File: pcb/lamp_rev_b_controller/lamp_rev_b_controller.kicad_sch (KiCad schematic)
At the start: 0 parts

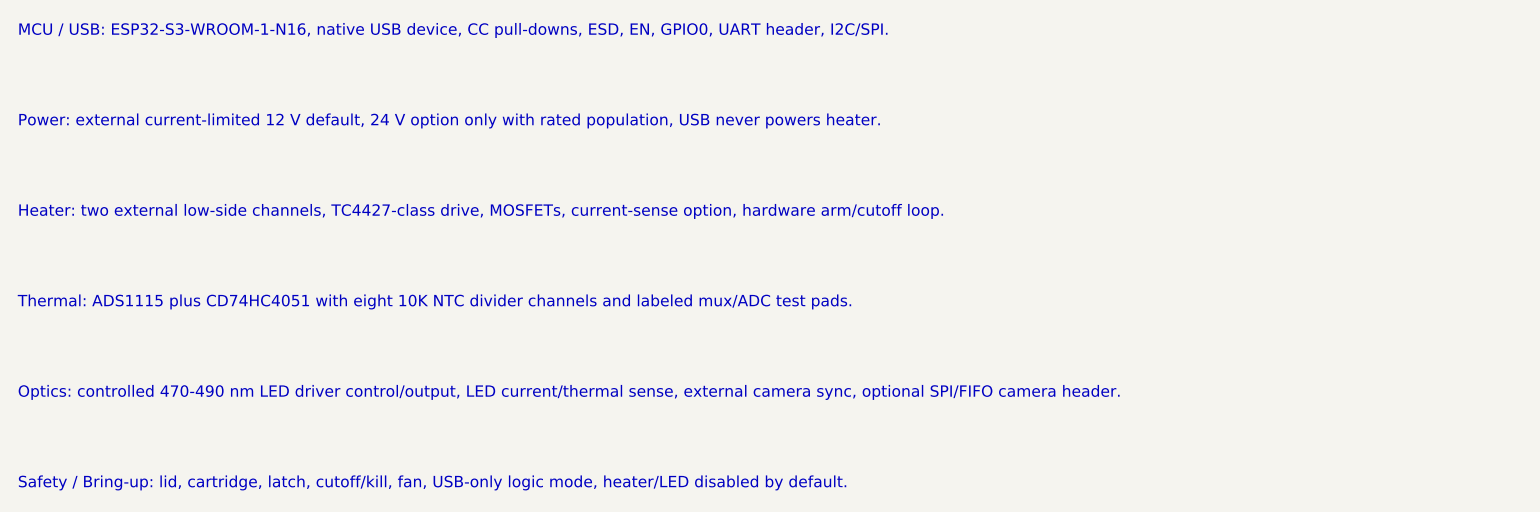
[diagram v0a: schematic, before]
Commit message: Resolve Rev B controller PCBA selection blockers
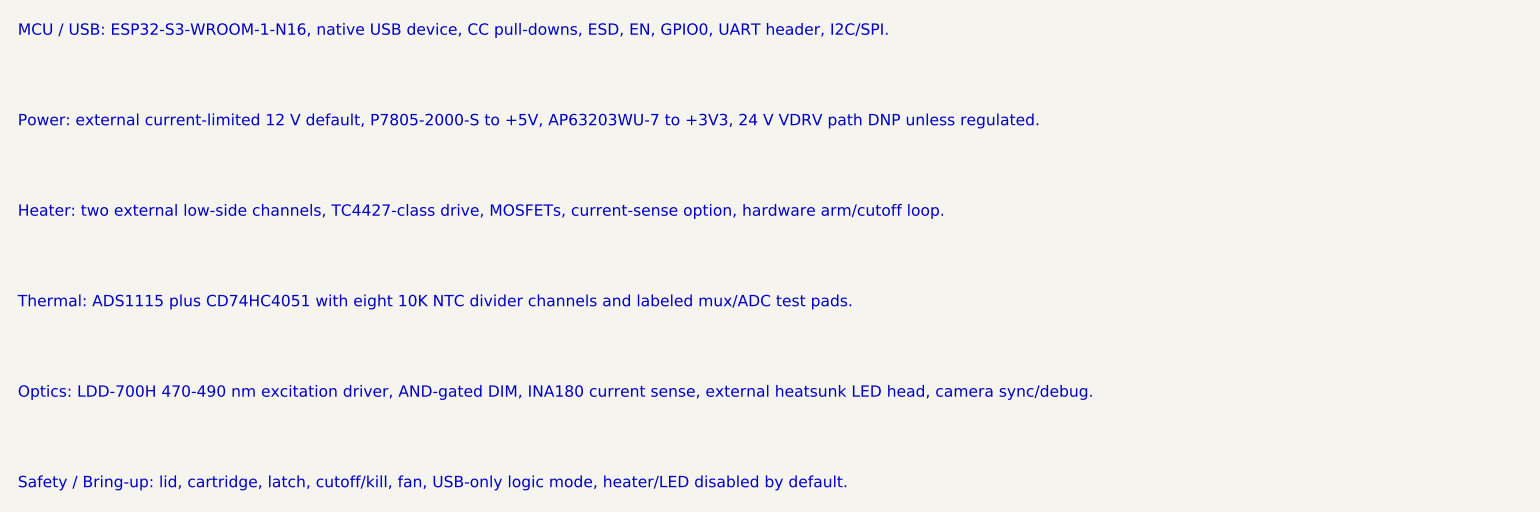
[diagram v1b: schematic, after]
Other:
- note added: "Optics: LDD-700H 470-490 nm excitation driver, AND-gated DIM, INA180 current sense, external heatsunk LED head, camera sync/debug."
- note added: "Power: external current-limited 12 V default, P7805-2000-S to +5V, AP63203WU-7 to +3V3, 24 V VDRV path DNP unless regulated."
- note removed: "Optics: controlled 470-490 nm LED driver control/output, LED current/thermal sense, external camera sync, optional SPI/FIFO camera header."
- note removed: "Power: external current-limited 12 V default, 24 V option only with rated population, USB never powers heater."
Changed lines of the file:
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@@
     (effects (font (size 1.27 1.27)) (justify left))
   )
-  (text "Power: external current-limited 12 V default, 24 V option only with rated population, USB never powers heater."
+  (text "Power: external current-limited 12 V default, P7805-2000-S to +5V, AP63203WU-7 to +3V3, 24 V VDRV path DNP unless regulated."
     (at 20.32 35.56 0)
     (effects (font (size 1.27 1.27)) (justify left))
@@
     (effects (font (size 1.27 1.27)) (justify left))
   )
-  (text "Optics: controlled 470-490 nm LED driver control/output, LED current/thermal sense, external camera sync, optional SPI/FIFO camera header."
+  (text "Optics: LDD-700H 470-490 nm excitation driver, AND-gated DIM, INA180 current sense, external heatsunk LED head, camera sync/debug."
     (at 20.32 66.04 0)
     (effects (font (size 1.27 1.27)) (justify left))

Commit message: Implement Rev B controller schematic capture gate
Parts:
- added C1: 22uF rail bulk, lcsc:C1206, symbol LF_CAPTURE_C1
- added C10: 100nF, lcsc:C0603, symbol LF_CAPTURE_C10
- added C11: 100nF, lcsc:C0603, symbol LF_CAPTURE_C11
- added C12: 100nF, lcsc:C0603, symbol LF_CAPTURE_C12
- added C13: 100nF, lcsc:C0603, symbol LF_CAPTURE_C13
- added C14: 100nF, lcsc:C0603, symbol LF_CAPTURE_C14
- added C15: 100nF, lcsc:C0603, symbol LF_CAPTURE_C15
- added C16: 100nF, lcsc:C0603, symbol LF_CAPTURE_C16
- added C17: 100nF, lcsc:C0603, symbol LF_CAPTURE_C17
- added C2: 22uF >=10V +5V buck output, lcsc:C1206, symbol LF_CAPTURE_C2
- added C3: 22uF AP63203 input, lcsc:C1206, symbol LF_CAPTURE_C3
- added C4: 22uF 50V VIN buck input, lcsc:C1206, symbol LF_CAPTURE_C4
- added C5: 22uF rail bulk, lcsc:C1206, symbol LF_CAPTURE_C5
- added C6: 22uF rail bulk, lcsc:C1206, symbol LF_CAPTURE_C6
- added C7: 22uF AP63203 output, lcsc:C1206, symbol LF_CAPTURE_C7
- added C8: 22uF AP63203 output, lcsc:C1206, symbol LF_CAPTURE_C8
- added C9: 100nF bootstrap, lcsc:C0603, symbol LF_CAPTURE_C9
- added D1: SMBJ18A footprint option, lcsc:SMB_L4.6-W3.6-LS5.3-RD, symbol LF_CAPTURE_D1
- added D2: LED0603 status, lcsc:LED0603-RD, symbol LF_CAPTURE_D2
- added D3: LED0603 status, lcsc:LED0603-RD, symbol LF_CAPTURE_D3
- added F1: RUEF500K/PTC, lcsc:FUSE2920, symbol LF_CAPTURE_F1
- added J1: TYPE-C 3.1 MT 16P, lcsc:USB-C-SMD_TYPE-C-USB-4, symbol LF_CAPTURE_J1
- added J10: 2-pin NTC header, lcsc:PINHEADER_1X02_2.54MM, symbol LF_CAPTURE_J10
- added J11: 2-pin NTC header, lcsc:PINHEADER_1X02_2.54MM, symbol LF_CAPTURE_J11
- added J12: DB128H-5.08-2P-BK-S, lcsc:TERM-BLOCK-5.08-2P, symbol LF_CAPTURE_J12
- added J13: DB128H-5.08-2P-BK-S, lcsc:TERM-BLOCK-5.08-2P, symbol LF_CAPTURE_J13
- added J15: DB128H-5.08-2P-BK-S, lcsc:TERM-BLOCK-5.08-2P, symbol LF_CAPTURE_J15
- added J16: LED NTC/ID header, lcsc:PINHEADER_1X04_2.54MM, symbol LF_CAPTURE_J16
- added J17: External camera sync header, lcsc:PINHEADER_1X06_2.54MM, symbol LF_CAPTURE_J17
- added J18: SPI/FIFO camera module header, lcsc:PINHEADER_2X06_2.54MM, symbol LF_CAPTURE_J18
- added J19: Lid/cartridge/cutoff interlock header, lcsc:PINHEADER_1X06_2.54MM, symbol LF_CAPTURE_J19
- added J2: DB128H-5.08-2P-BK-S, lcsc:TERM-BLOCK-5.08-2P, symbol LF_CAPTURE_J2
- added J20: Fan PWM/tach header, lcsc:PINHEADER_1X04_2.54MM, symbol LF_CAPTURE_J20
- added J21: 2x3 UART/programming header, lcsc:PINHEADER_2X03_2.54MM, symbol LF_CAPTURE_J21
- added J22: I2C expansion header, lcsc:PINHEADER_1X04_2.54MM, symbol LF_CAPTURE_J22
- added J23: Analog optical diagnostic header, lcsc:PINHEADER_1X06_2.54MM, symbol LF_CAPTURE_J23
- added J4: 2-pin NTC header, lcsc:PINHEADER_1X02_2.54MM, symbol LF_CAPTURE_J4
- added J5: 2-pin NTC header, lcsc:PINHEADER_1X02_2.54MM, symbol LF_CAPTURE_J5
- added J6: 2-pin NTC header, lcsc:PINHEADER_1X02_2.54MM, symbol LF_CAPTURE_J6
- added J7: 2-pin NTC header, lcsc:PINHEADER_1X02_2.54MM, symbol LF_CAPTURE_J7
- added J8: 2-pin NTC header, lcsc:PINHEADER_1X02_2.54MM, symbol LF_CAPTURE_J8
- added J9: 2-pin NTC header, lcsc:PINHEADER_1X02_2.54MM, symbol LF_CAPTURE_J9
- added L1: Wurth 74439346068 6.8uH shielded inductor, lcsc:IND_74439346068, symbol LF_CAPTURE_L1
- added Q1: IRLB3813PBF TO-220 12V prototype, lcsc:TO-220-3_VERTICAL, symbol LF_CAPTURE_Q1
- added Q2: IRLB3813PBF TO-220 12V prototype, lcsc:TO-220-3_VERTICAL, symbol LF_CAPTURE_Q2
- added R1: 5.1k, lcsc:R0805, symbol LF_CAPTURE_R1
- added R10: 10k 0.1%, lcsc:R0805, symbol LF_CAPTURE_R10
- added R11: 10k 0.1%, lcsc:R0805, symbol LF_CAPTURE_R11
- added R12: 10k 0.1%, lcsc:R0805, symbol LF_CAPTURE_R12
- added R13: 10k 0.1%, lcsc:R0805, symbol LF_CAPTURE_R13
- added R14: 10k 0.1%, lcsc:R0805, symbol LF_CAPTURE_R14
- added R15: 10k 0.1%, lcsc:R0805, symbol LF_CAPTURE_R15
- added R16: 10k 0.1%, lcsc:R0805, symbol LF_CAPTURE_R16
- added R17: 10k 0.1%, lcsc:R0805, symbol LF_CAPTURE_R17
- added R2: 5.1k, lcsc:R0805, symbol LF_CAPTURE_R2
- added R20: 33R, lcsc:R0805, symbol LF_CAPTURE_R20
- added R21: 33R, lcsc:R0805, symbol LF_CAPTURE_R21
- added R22: 10k, lcsc:R0805, symbol LF_CAPTURE_R22
- added R23: 10k, lcsc:R0805, symbol LF_CAPTURE_R23
- added R24: 10k, lcsc:R0805, symbol LF_CAPTURE_R24
- added R25: 50mR DNP option, lcsc:R0805, symbol LF_CAPTURE_R25
- added R26: 50mR DNP option, lcsc:R0805, symbol LF_CAPTURE_R26
- added R3: 100k/100k VBUS sense, lcsc:R0805, symbol LF_CAPTURE_R3
- added R30: 1k, lcsc:R0805, symbol LF_CAPTURE_R30
- added R31: 1k, lcsc:R0805, symbol LF_CAPTURE_R31
- added R4: 100k/100k VBUS sense, lcsc:R0805, symbol LF_CAPTURE_R4
- added R40: 4.7k, lcsc:R0805, symbol LF_CAPTURE_R40
- added R41: 4.7k, lcsc:R0805, symbol LF_CAPTURE_R41
- added R42: 4.7k, lcsc:R0805, symbol LF_CAPTURE_R42
- added R43: 4.7k, lcsc:R0805, symbol LF_CAPTURE_R43
- added R44: 4.7k, lcsc:R0805, symbol LF_CAPTURE_R44
- added R45: 4.7k, lcsc:R0805, symbol LF_CAPTURE_R45
- added R46: 4.7k, lcsc:R0805, symbol LF_CAPTURE_R46
- added R47: 4.7k, lcsc:R0805, symbol LF_CAPTURE_R47
- added R48: 10k, lcsc:R0805, symbol LF_CAPTURE_R48
- added R49: 10k, lcsc:R0805, symbol LF_CAPTURE_R49
- added R50: 100R LED DIM series, lcsc:R0805, symbol LF_CAPTURE_R50
- added R51: 100k LED DIM pulldown, lcsc:R0805, symbol LF_CAPTURE_R51
- added R52: 0R LED_SUPPLY feed link from VIN_PROTECTED, lcsc:R0805, symbol LF_CAPTURE_R52
- added R53: 0.1R 1% >=1W LED current shunt, lcsc:R2512, symbol LF_CAPTURE_R53
- added R54: 10k LED_FAULT_N pull-up, lcsc:R0805, symbol LF_CAPTURE_R54
- added TP_3V3: test point +3V3, lcsc:TESTPOINT_SMD_1.5MM, symbol LF_CAPTURE_TP_3V3
- added TP_3V3A: test point +3V3_ANA, lcsc:TESTPOINT_SMD_1.5MM, symbol LF_CAPTURE_TP_3V3A
- added TP_5V: test point +5V, lcsc:TESTPOINT_SMD_1.5MM, symbol LF_CAPTURE_TP_5V
- added TP_ADS_AIN0: test point ADS_AIN0, lcsc:TESTPOINT_SMD_1.5MM, symbol LF_CAPTURE_TP_ADS_AIN0
- added TP_ADS_AIN1: test point ADS_AIN1, lcsc:TESTPOINT_SMD_1.5MM, symbol LF_CAPTURE_TP_ADS_AIN1
- added TP_ADS_AIN2: test point ADS_AIN2, lcsc:TESTPOINT_SMD_1.5MM, symbol LF_CAPTURE_TP_ADS_AIN2
- added TP_ADS_AIN3: test point ADS_AIN3, lcsc:TESTPOINT_SMD_1.5MM, symbol LF_CAPTURE_TP_ADS_AIN3
- added TP_AUX_ANALOG: test point AUX_ANALOG_IN, lcsc:TESTPOINT_SMD_1.5MM, symbol LF_CAPTURE_TP_AUX_ANALOG
- added TP_BOOT: test point ESP_GPIO0_BOOT, lcsc:TESTPOINT_SMD_1.5MM, symbol LF_CAPTURE_TP_BOOT
- added TP_CAM_CS: test point CAM_CS_N, lcsc:TESTPOINT_SMD_1.5MM, symbol LF_CAPTURE_TP_CAM_CS
- added TP_CAM_FRAME: test point CAM_FRAME_INT, lcsc:TESTPOINT_SMD_1.5MM, symbol LF_CAPTURE_TP_CAM_FRAME
- added TP_CAM_PWDN: test point CAM_PWDN_N, lcsc:TESTPOINT_SMD_1.5MM, symbol LF_CAPTURE_TP_CAM_PWDN
- added TP_CAM_RESET: test point CAM_RESET_N, lcsc:TESTPOINT_SMD_1.5MM, symbol LF_CAPTURE_TP_CAM_RESET
- added TP_CART: test point CART_PRESENT_N, lcsc:TESTPOINT_SMD_1.5MM, symbol LF_CAPTURE_TP_CART
- added TP_CUTOFF: test point AUX_IO0_THERMAL_CUTOFF_OK, lcsc:TESTPOINT_SMD_1.5MM, symbol LF_CAPTURE_TP_CUTOFF
- added TP_EN: test point ESP_EN, lcsc:TESTPOINT_SMD_1.5MM, symbol LF_CAPTURE_TP_EN
- added TP_EXPOSURE: test point EXPOSURE_ACTIVE_IN, lcsc:TESTPOINT_SMD_1.5MM, symbol LF_CAPTURE_TP_EXPOSURE
- added TP_FAN_PWM: test point FAN_PWM, lcsc:TESTPOINT_SMD_1.5MM, symbol LF_CAPTURE_TP_FAN_PWM
- added TP_FAN_TACH: test point FAN_TACH, lcsc:TESTPOINT_SMD_1.5MM, symbol LF_CAPTURE_TP_FAN_TACH
- added TP_FAULT: test point STATUS_FAULT_LED, lcsc:TESTPOINT_SMD_1.5MM, symbol LF_CAPTURE_TP_FAULT
- added TP_FRAME_TRIG: test point FRAME_TRIG_OUT, lcsc:TESTPOINT_SMD_1.5MM, symbol LF_CAPTURE_TP_FRAME_TRIG
- added TP_GND: test point GND, lcsc:TESTPOINT_SMD_1.5MM, symbol LF_CAPTURE_TP_GND
- added TP_HEATER0_GATE: test point HEATER0_GATE, lcsc:TESTPOINT_SMD_1.5MM, symbol LF_CAPTURE_TP_HEATER0_GATE
- added TP_HEATER0_LOW: test point HEATER0_LOW, lcsc:TESTPOINT_SMD_1.5MM, symbol LF_CAPTURE_TP_HEATER0_LOW
- added TP_HEATER0_PWM: test point HEATER0_PWM, lcsc:TESTPOINT_SMD_1.5MM, symbol LF_CAPTURE_TP_HEATER0_PWM
- added TP_HEATER1_GATE: test point HEATER1_GATE, lcsc:TESTPOINT_SMD_1.5MM, symbol LF_CAPTURE_TP_HEATER1_GATE
- added TP_HEATER1_LOW: test point HEATER1_LOW, lcsc:TESTPOINT_SMD_1.5MM, symbol LF_CAPTURE_TP_HEATER1_LOW
- added TP_HEATER1_PWM: test point HEATER1_PWM, lcsc:TESTPOINT_SMD_1.5MM, symbol LF_CAPTURE_TP_HEATER1_PWM
- added TP_HEATER_ARM: test point HEATER_ARM, lcsc:TESTPOINT_SMD_1.5MM, symbol LF_CAPTURE_TP_HEATER_ARM
- added TP_HEATER_SENSE: test point HEATER_SUPPLY_SENSE, lcsc:TESTPOINT_SMD_1.5MM, symbol LF_CAPTURE_TP_HEATER_SENSE
- added TP_I2C_SCL: test point I2C_SCL, lcsc:TESTPOINT_SMD_1.5MM, symbol LF_CAPTURE_TP_I2C_SCL
- added TP_I2C_SDA: test point I2C_SDA, lcsc:TESTPOINT_SMD_1.5MM, symbol LF_CAPTURE_TP_I2C_SDA
- added TP_LATCH: test point LATCH_LOCKED_N, lcsc:TESTPOINT_SMD_1.5MM, symbol LF_CAPTURE_TP_LATCH
- added TP_LED_EN: test point LED_EXC_EN, lcsc:TESTPOINT_SMD_1.5MM, symbol LF_CAPTURE_TP_LED_EN
- added TP_LED_PWM: test point LED_EXC_PWM, lcsc:TESTPOINT_SMD_1.5MM, symbol LF_CAPTURE_TP_LED_PWM
- added TP_LED_SENSE: test point LED_CURRENT_SENSE, lcsc:TESTPOINT_SMD_1.5MM, symbol LF_CAPTURE_TP_LED_SENSE
- added TP_LED_SUPPLY: test point LED_SUPPLY, lcsc:TESTPOINT_SMD_1.5MM, symbol LF_CAPTURE_TP_LED_SUPPLY
- added TP_LED_SYNC: test point LED_SYNC_OUT, lcsc:TESTPOINT_SMD_1.5MM, symbol LF_CAPTURE_TP_LED_SYNC
- added TP_LID: test point LID_CLOSED_N, lcsc:TESTPOINT_SMD_1.5MM, symbol LF_CAPTURE_TP_LID
- added TP_RUN: test point STATUS_RUN_LED, lcsc:TESTPOINT_SMD_1.5MM, symbol LF_CAPTURE_TP_RUN
- added TP_SD_CS: test point SD_CS_N, lcsc:TESTPOINT_SMD_1.5MM, symbol LF_CAPTURE_TP_SD_CS
- added TP_SPARE42: test point SPARE_GPIO42, lcsc:TESTPOINT_SMD_1.5MM, symbol LF_CAPTURE_TP_SPARE42
- added TP_SPI_MISO: test point SPI_MISO, lcsc:TESTPOINT_SMD_1.5MM, symbol LF_CAPTURE_TP_SPI_MISO
- added TP_SPI_MOSI: test point SPI_MOSI, lcsc:TESTPOINT_SMD_1.5MM, symbol LF_CAPTURE_TP_SPI_MOSI
- added TP_SPI_SCLK: test point SPI_SCLK, lcsc:TESTPOINT_SMD_1.5MM, symbol LF_CAPTURE_TP_SPI_SCLK
- added TP_THERM_EN: test point THERM_MUX_EN_N, lcsc:TESTPOINT_SMD_1.5MM, symbol LF_CAPTURE_TP_THERM_EN
- added TP_THERM_OUT: test point THERM_MUX_OUT, lcsc:TESTPOINT_SMD_1.5MM, symbol LF_CAPTURE_TP_THERM_OUT
- added TP_THERM_S0: test point THERM_MUX_S0, lcsc:TESTPOINT_SMD_1.5MM, symbol LF_CAPTURE_TP_THERM_S0
- added TP_THERM_S1: test point THERM_MUX_S1, lcsc:TESTPOINT_SMD_1.5MM, symbol LF_CAPTURE_TP_THERM_S1
- added TP_THERM_S2: test point THERM_MUX_S2, lcsc:TESTPOINT_SMD_1.5MM, symbol LF_CAPTURE_TP_THERM_S2
- added TP_UART_RX: test point UART0_RXD, lcsc:TESTPOINT_SMD_1.5MM, symbol LF_CAPTURE_TP_UART_RX
- added TP_UART_TX: test point UART0_TXD, lcsc:TESTPOINT_SMD_1.5MM, symbol LF_CAPTURE_TP_UART_TX
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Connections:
- new net +3V3: C7.1 (+3V3), C8.1 (+3V3), D2.2 (+3V3), D3.2 (+3V3), J17.2 (+3V3), J18.3 (SPI_SCLK), J19.5 (+3V3), J21.2 (+3V3), J22.4 (GND), L1.2 (+3V3), R40.2 (+3V3), R41.2 (+3V3)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
- new net +3V3_ANA: C5.1 (+3V3_ANA), J16.4 (GND), J23.3 (ADS_AIN3), TP_3V3A.1 (+3V3_ANA), U5.1 (THERM_CH_4)
- new net +5V: C2.1 (+5V), C3.1 (+5V), J20.4 (GND), TP_5V.1 (+5V), U3.2 (+5V), U3.6 (3V3_BST)
- new net 3V3_BST: C9.1 (3V3_BST), U3.4 (+5V)
- new net 3V3_SW: C9.2 (3V3_SW), L1.1 (3V3_SW), U3.5 (3V3_SW)
- new net ADS_AIN0: TP_ADS_AIN0.1 (ADS_AIN0), U4.1 (GND)
- new net ADS_AIN1: TP_ADS_AIN1.1 (ADS_AIN1), U4.9 (I2C_SDA)
- new net ADS_AIN2: TP_ADS_AIN2.1 (ADS_AIN2), U4.8 (+3V3)
- new net ADS_AIN3: J23.1 (+3V3_ANA), TP_ADS_AIN3.1 (ADS_AIN3), U4.7 (ADS_AIN3)
- new net AUX_ANALOG_IN: J16.1 (THERM_CH_5), J23.6 (I2C_SCL), TP_AUX_ANALOG.1 (AUX_ANALOG_IN)
- new net AUX_IO0_THERMAL_CUTOFF_OK: J19.6 (GND), R47.1 (AUX_IO0_THERMAL_CUTOFF_OK), TP_CUTOFF.1 (AUX_IO0_THERMAL_CUTOFF_OK), U1.6 (THERM_MUX_S2)
- new net CAM_CS_N: J18.7 (CAM_FRAME_INT), R42.1 (CAM_CS_N), TP_CAM_CS.1 (CAM_CS_N), U1.17 (SPI_SCLK)
- new net CAM_FRAME_INT: J18.6 (CAM_CS_N), TP_CAM_FRAME.1 (CAM_FRAME_INT), U1.16 (NC_16)
- new net CAM_PWDN_N: J18.4 (SPI_MOSI), TP_CAM_PWDN.1 (CAM_PWDN_N), U1.15 (NC_15)
- new net CAM_RESET_N: J18.5 (SPI_MISO), TP_CAM_RESET.1 (CAM_RESET_N), U1.30 (LID_CLOSED_N)
- new net CART_PRESENT_N: J19.2 (CART_PRESENT_N), R45.1 (CART_PRESENT_N), TP_CART.1 (CART_PRESENT_N), U1.7 (LED_EXC_PWM)
- new net ESP_EN: J21.5 (ESP_EN), R48.1 (ESP_EN), TP_EN.1 (ESP_EN), U1.9 (HEATER_ARM)
- new net ESP_GPIO0_BOOT: J21.4 (UART0_RXD), R49.1 (ESP_GPIO0_BOOT), TP_BOOT.1 (ESP_GPIO0_BOOT), U1.10 (HEATER0_PWM)
- new net EXPOSURE_ACTIVE_IN: J17.6 (SPARE_GPIO42), TP_EXPOSURE.1 (EXPOSURE_ACTIVE_IN)
- new net FAN_PWM: J20.2 (FAN_TACH), TP_FAN_PWM.1 (FAN_PWM)
- new net FAN_TACH: J20.1 (FAN_PWM), TP_FAN_TACH.1 (FAN_TACH)
- new net FRAME_TRIG_OUT: J17.1 (GND), TP_FRAME_TRIG.1 (FRAME_TRIG_OUT), U1.12 (THERM_MUX_EN_N)
- new net GND: C1.2 (GND), C2.2 (GND), C3.2 (GND), C4.2 (GND), C5.2 (GND), C6.2 (GND), C7.2 (GND), C8.2 (GND), D1.2 (GND), J1.16 (GND), J1.A12B1 (GND), J1.A5 (USB_CC1)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
- new net GND_EP: U1.34 (STATUS_FAULT_LED)
- new net HEATER0_GATE: Q1.2 (HEATER0_LOW), R20.2 (HEATER0_GATE), R23.1 (HEATER0_GATE), TP_HEATER0_GATE.1 (HEATER0_GATE), U6.6 (VDRV)
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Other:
- note added: "Connectivity source: parts.toml + placement.toml + pin_nets.toml + placement test points."
- note added: "Every assigned footprint pad is tied to a global net label; unassigned footprint pads are explicit no-connects."
- note added: "External high-power LED remains off-board on J15; LDD-700H is manual/THT no-substitution for first articles."
- note removed: "Heater: two external low-side channels, TC4427-class drive, MOSFETs, current-sense option, hardware arm/cutoff loop."
- note removed: "MCU / USB: ESP32-S3-WROOM-1-N16, native USB device, CC pull-downs, ESD, EN, GPIO0, UART header, I2C/SPI."
- note removed: "Optics: LDD-700H 470-490 nm excitation driver, AND-gated DIM, INA180 current sense, external heatsunk LED head, camera sync/debug."
- note removed: "Power: external current-limited 12 V default, P7805-2000-S to +5V, AP63203WU-7 to +3V3, 24 V VDRV path DNP unless regulated."
- note removed: "Safety / Bring-up: lid, cartridge, latch, cutoff/kill, fan, USB-only logic mode, heater/LED disabled by default."
- note removed: "Thermal: ADS1115 plus CD74HC4051 with eight 10K NTC divider channels and labeled mux/ADC test pads."

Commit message: Implement Rev B source-boundary route pass
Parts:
- added U10: INA180A1IDBVR gain 20 LED current sense, lcsc:SOT-23-5, symbol LF_CAPTURE_U10
- added U8: Mean Well LDD-700H 700mA CC buck LED driver; LDD-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, lcsc:MEANWELL_LDD-300-1000H_THT, symbol LF_CAPTURE_U8
- added U9: SN74LVC1G08DBVR LED_EXC_PWM AND LED_EXC_EN, lcsc:SOT-23-5, symbol LF_CAPTURE_U9
- FB1: renamed from J1; value TYPE-C 3.1 MT 16P -> 0805 ferrite bead / approved analog rail link from +3V3 to +3V3_ANA; footprint lcsc:USB-C-SMD_TYPE-C-USB-4 -> lcsc:R0805; symbol LF_CAPTURE_J1 -> LF_CAPTURE_FB1; LCSC Part C168688 -> select real 0805 ferrite before fab; 0R only as documented 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; Notes USB-C UFP/device port. -> Analog +3V3 source filter/link; pin 1 is logic +3V3 source,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
- J1: renamed from J2; value DB128H-5.08-2P-BK-S -> TYPE-C 3.1 MT 16P; footprint lcsc:TERM-BLOCK-5.08-2P -> lcsc:USB-C-SMD_TYPE-C-USB-4; symbol LF_CAPTURE_J2 -> LF_CAPTURE_J1; LCSC Part C430605 -> C168688; Notes External 12/24 V input terminal. -> USB-C UFP/device port.
- J10: renamed from J11; symbol LF_CAPTURE_J11 -> LF_CAPTURE_J10; Notes THERM_CH_7 NTC header. -> THERM_CH_6 NTC header.
- J11: renamed from J12; value DB128H-5.08-2P-BK-S -> 2-pin NTC header; footprint lcsc:TERM-BLOCK-5.08-2P -> lcsc:PINHEADER_1X02_2.54MM; symbol LF_CAPTURE_J12 -> LF_CAPTURE_J11; LCSC Part C430605 -> MANUAL; Notes Primary heater output terminal. -> THERM_CH_7 NTC header.
- J12: renamed from J13; symbol LF_CAPTURE_J13 -> LF_CAPTURE_J12; Notes Secondary heater output terminal. -> Primary heater output terminal.
- J13: renamed from J15; symbol LF_CAPTURE_J15 -> LF_CAPTURE_J13; Notes High-current off-board LED output. -> Secondary heater output terminal.
- J15: renamed from J16; value LED NTC/ID header -> DB128H-5.08-2P-BK-S; footprint lcsc:PINHEADER_1X04_2.54MM -> lcsc:TERM-BLOCK-5.08-2P; symbol LF_CAPTURE_J16 -> LF_CAPTURE_J15; LCSC Part MANUAL -> C430605; Notes LED heatsink NTC / ID header. -> High-current off-board LED output.
- J16: renamed from J17; value External camera sync header -> LED NTC/ID header; footprint lcsc:PINHEADER_1X06_2.54MM -> lcsc:PINHEADER_1X04_2.54MM; symbol LF_CAPTURE_J17 -> LF_CAPTURE_J16; Notes External camera host sync header. -> LED heatsink NTC / ID header.
- J17: renamed from J18; value SPI/FIFO camera module header -> External camera sync header; footprint lcsc:PINHEADER_2X06_2.54MM -> lcsc:PINHEADER_1X06_2.54MM; symbol LF_CAPTURE_J18 -> LF_CAPTURE_J17; Notes Optional SPI/FIFO camera module header. -> External camera host sync header.
- J18: renamed from J19; value Lid/cartridge/cutoff interlock header -> SPI/FIFO camera module header; footprint lcsc:PINHEADER_1X06_2.54MM -> lcsc:PINHEADER_2X06_2.54MM; symbol LF_CAPTURE_J19 -> LF_CAPTURE_J18; Notes Lid/cartridge/cutoff interlock header. -> Optional SPI/FIFO camera module header.
- J19: renamed from J20; value Fan PWM/tach header -> Lid/cartridge/cutoff interlock header; footprint lcsc:PINHEADER_1X04_2.54MM -> lcsc:PINHEADER_1X06_2.54MM; symbol LF_CAPTURE_J20 -> LF_CAPTURE_J19; Notes Optional fan PWM/tach header. -> Lid/cartridge/cutoff interlock header.
- J2: renamed from J4; value 2-pin NTC header -> DB128H-5.08-2P-BK-S; footprint lcsc:PINHEADER_1X02_2.54MM -> lcsc:TERM-BLOCK-5.08-2P; symbol LF_CAPTURE_J4 -> LF_CAPTURE_J2; LCSC Part MANUAL -> C430605; Notes THERM_CH_0 NTC header. -> External 12/24 V input terminal.
- J20: renamed from J21; value 2x3 UART/programming header -> Fan PWM/tach header; footprint lcsc:PINHEADER_2X03_2.54MM -> lcsc:PINHEADER_1X04_2.54MM; symbol LF_CAPTURE_J21 -> LF_CAPTURE_J20; Notes 2x3 UART/programming header; +3V3 is sense only unless expl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 -> Optional fan PWM/tach header.
- J21: renamed from J22; value I2C expansion header -> 2x3 UART/programming header; footprint lcsc:PINHEADER_1X04_2.54MM -> lcsc:PINHEADER_2X03_2.54MM; symbol LF_CAPTURE_J22 -> LF_CAPTURE_J21; Notes I2C expansion. -> 2x3 UART/programming header; +3V3 is sense only unless expl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
- J22: renamed from J23; value Analog optical diagnostic header -> I2C expansion header; footprint lcsc:PINHEADER_1X06_2.54MM -> lcsc:PINHEADER_1X04_2.54MM; symbol LF_CAPTURE_J23 -> LF_CAPTURE_J22; Notes Analog optical diagnostic header. -> I2C expansion.
- J23: renamed from L1; value Wurth 74439346068 6.8uH shielded inductor -> Analog optical diagnostic header; footprint lcsc:IND_74439346068 -> lcsc:PINHEADER_1X06_2.54MM; symbol LF_CAPTURE_L1 -> LF_CAPTURE_J23; LCSC Part C2041388 -> MANUAL; Notes Wurth 74439346068 AP63203 buck inductor. -> Analog optical diagnostic header.
- J24: renamed from Q1; value IRLB3813PBF TO-220 12V prototype -> DB128H-5.08-2P high-current heater cutoff loop/link; footprint lcsc:TO-220-3_VERTICAL -> lcsc:TERM-BLOCK-5.08-2P; symbol LF_CAPTURE_Q1 -> LF_CAPTURE_J24; LCSC Part DigiKey IRLB3813PBF-ND -> C430605; Notes HEATER0 low-side MOSFET, TO-220 pinout gate/drain/source. -> High-current external heater cutoff loop terminal.
- J4: renamed from J5; symbol LF_CAPTURE_J5 -> LF_CAPTURE_J4; Notes THERM_CH_1 NTC header. -> THERM_CH_0 NTC header.
- J5: renamed from J6; symbol LF_CAPTURE_J6 -> LF_CAPTURE_J5; Notes THERM_CH_2 NTC header. -> THERM_CH_1 NTC header.
- J6: renamed from J7; symbol LF_CAPTURE_J7 -> LF_CAPTURE_J6; Notes THERM_CH_3 NTC header. -> THERM_CH_2 NTC header.
- J7: renamed from J8; symbol LF_CAPTURE_J8 -> LF_CAPTURE_J7; Notes THERM_CH_4 NTC header. -> THERM_CH_3 NTC header.
- J8: renamed from J9; symbol LF_CAPTURE_J9 -> LF_CAPTURE_J8; Notes THERM_CH_5 NTC header. -> THERM_CH_4 NTC header.
- J9: renamed from J10; symbol LF_CAPTURE_J10 -> LF_CAPTURE_J9; Notes THERM_CH_6 NTC header. -> THERM_CH_5 NTC header.
- L1: renamed from Q2; value IRLB3813PBF TO-220 12V prototype -> Wurth 74439346068 6.8uH shielded inductor; footprint lcsc:TO-220-3_VERTICAL -> lcsc:IND_74439346068; symbol LF_CAPTURE_Q2 -> LF_CAPTURE_L1; LCSC Part DigiKey IRLB3813PBF-ND -> C2041388; Notes HEATER1 low-side MOSFET, TO-220 pinout gate/drain/source. -> Wurth 74439346068 AP63203 buck inductor.
- Q1: renamed from R1; value 5.1k -> IRLB3813PBF TO-220 12V prototype; footprint lcsc:R0805 -> lcsc:TO-220-3_VERTICAL; symbol LF_CAPTURE_R1 -> LF_CAPTURE_Q1; LCSC Part C27834 -> DigiKey IRLB3813PBF-ND; Notes USB-C CC1 5.1k sink pull-down. -> HEATER0 low-side MOSFET, TO-220 pinout gate/drain/source.
- Q2: renamed from R2; value 5.1k -> IRLB3813PBF TO-220 12V prototype; footprint lcsc:R0805 -> lcsc:TO-220-3_VERTICAL; symbol LF_CAPTURE_R2 -> LF_CAPTURE_Q2; LCSC Part C27834 -> DigiKey IRLB3813PBF-ND; Notes USB-C CC2 5.1k sink pull-down. -> HEATER1 low-side MOSFET, TO-220 pinout gate/drain/source.
- R1: renamed from R3; value 100k/100k VBUS sense -> 5.1k; symbol LF_CAPTURE_R3 -> LF_CAPTURE_R1; LCSC Part C17514 -> C27834; Notes Upper VBUS sense divider. -> USB-C CC1 5.1k sink pull-down.
- R10: renamed from R12; symbol LF_CAPTURE_R12 -> LF_CAPTURE_R10
- R11: renamed from R13; symbol LF_CAPTURE_R13 -> LF_CAPTURE_R11
- R12: renamed from R14; symbol LF_CAPTURE_R14 -> LF_CAPTURE_R12
- R13: renamed from R15; symbol LF_CAPTURE_R15 -> LF_CAPTURE_R13
- R14: renamed from R16; symbol LF_CAPTURE_R16 -> LF_CAPTURE_R14
- R15: renamed from R17; symbol LF_CAPTURE_R17 -> LF_CAPTURE_R15
- R16: renamed from R20; value 33R -> 10k 0.1%; symbol LF_CAPTURE_R20 -> LF_CAPTURE_R16; LCSC Part C17408 -> DigiKey A105700-ND; Notes HEATER0 gate series resistor. -> (none)
- R17: renamed from R21; value 33R -> 10k 0.1%; symbol LF_CAPTURE_R21 -> LF_CAPTURE_R17; LCSC Part C17408 -> DigiKey A105700-ND; Notes HEATER1 gate series resistor. -> (none)
- R2: renamed from R4; value 100k/100k VBUS sense -> 5.1k; symbol LF_CAPTURE_R4 -> LF_CAPTURE_R2; LCSC Part C17514 -> C27834; Notes Lower VBUS sense divider. -> USB-C CC2 5.1k sink pull-down.
- R20: renamed from R22; value 10k -> 33R; symbol LF_CAPTURE_R22 -> LF_CAPTURE_R20; LCSC Part C17414 -> C17408; Notes HEATER_ARM pulldown. -> HEATER0 gate series resistor.
- R21: renamed from R23; value 10k -> 33R; symbol LF_CAPTURE_R23 -> LF_CAPTURE_R21; LCSC Part C17414 -> C17408; Notes HEATER0 gate pulldown. -> HEATER1 gate series resistor.
- R22: renamed from R24; symbol LF_CAPTURE_R24 -> LF_CAPTURE_R22; Notes HEATER1 gate pulldown. -> HEATER_ARM pulldown.
- R23: renamed from R25; value 50mR DNP option -> 10k; symbol LF_CAPTURE_R25 -> LF_CAPTURE_R23; LCSC Part DNP -> C17414; Notes HEATER0 optional current shunt. -> HEATER0 gate pulldown.
- R24: renamed from R26; value 50mR DNP option -> 10k; symbol LF_CAPTURE_R26 -> LF_CAPTURE_R24; LCSC Part DNP -> C17414; Notes HEATER1 optional current shunt. -> HEATER1 gate pulldown.
- R25: renamed from R30; value 1k -> 50mR DNP option; symbol LF_CAPTURE_R30 -> LF_CAPTURE_R25; LCSC Part C17513 -> DNP; Notes Run LED current limit. -> HEATER0 optional current shunt.
- R26: renamed from R31; value 1k -> 50mR DNP option; symbol LF_CAPTURE_R31 -> LF_CAPTURE_R26; LCSC Part C17513 -> DNP; Notes Fault LED current limit. -> HEATER1 optional current shunt.
- R3: renamed from R10; value 10k 0.1% -> 100k/100k VBUS sense; symbol LF_CAPTURE_R10 -> LF_CAPTURE_R3; LCSC Part DigiKey A105700-ND -> C17514; Notes (none) -> Upper VBUS sense divider.
- R30: renamed from R40; value 4.7k -> 1k; symbol LF_CAPTURE_R40 -> LF_CAPTURE_R30; LCSC Part C17673 -> C17513; Notes I2C SDA pull-up. -> Run LED current limit.
- R31: renamed from R41; value 4.7k -> 1k; symbol LF_CAPTURE_R41 -> LF_CAPTURE_R31; LCSC Part C17673 -> C17513; Notes I2C SCL pull-up. -> Fault LED current limit.
- R4: renamed from R11; value 10k 0.1% -> 100k/100k VBUS sense; symbol LF_CAPTURE_R11 -> LF_CAPTURE_R4; LCSC Part DigiKey A105700-ND -> C17514; Notes (none) -> Lower VBUS sense divider.
- R40: renamed from R42; symbol LF_CAPTURE_R42 -> LF_CAPTURE_R40; Notes CAM_CS_N pull-up. -> I2C SDA pull-up.
- R41: renamed from R43; symbol LF_CAPTURE_R43 -> LF_CAPTURE_R41; Notes SD_CS_N pull-up. -> I2C SCL pull-up.
- R42: renamed from R44; symbol LF_CAPTURE_R44 -> LF_CAPTURE_R42; Notes Lid switch pull-up. -> CAM_CS_N pull-up.
- R43: renamed from R45; symbol LF_CAPTURE_R45 -> LF_CAPTURE_R43; Notes Cartridge switch pull-up. -> SD_CS_N pull-up.
- R44: renamed from R46; symbol LF_CAPTURE_R46 -> LF_CAPTURE_R44; Notes Latch switch pull-up. -> Lid switch pull-up.
- R45: renamed from R47; symbol LF_CAPTURE_R47 -> LF_CAPTURE_R45; Notes Thermal cutoff status pull-up. -> Cartridge switch pull-up.
- R46: renamed from R48; value 10k -> 4.7k; symbol LF_CAPTURE_R48 -> LF_CAPTURE_R46; LCSC Part C17414 -> C17673; Notes ESP_EN pull-up. -> Latch switch pull-up.
- R47: renamed from R49; value 10k -> 4.7k; symbol LF_CAPTURE_R49 -> LF_CAPTURE_R47; LCSC Part C17414 -> C17673; Notes GPIO0 boot pull-up. -> Thermal cutoff status pull-up.
- R48: renamed from R50; value 100R LED DIM series -> 10k; symbol LF_CAPTURE_R50 -> LF_CAPTURE_R48; LCSC Part C17408 -> C17414; Notes LED DIM series resistor from AND gate to LDD DIM. -> ESP_EN pull-up.
- R49: renamed from R51; value 100k LED DIM pulldown -> 10k; symbol LF_CAPTURE_R51 -> LF_CAPTURE_R49; LCSC Part C17514 -> C17414; Notes LED DIM pulldown. -> GPIO0 boot pull-up.
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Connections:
- net +3V3: now also FB1.1 (+3V3), J17.2 (+3V3), J18.3 (SPI_SCLK), J19.5 (+3V3), J21.2 (+3V3), J22.4 (GND), L1.2 (+3V3), R48.2 (+3V3), R49.2 (+3V3), R54.2 (+3V3), TP_3V3.1 (+3V3), U1.18 (SPI_MOSI)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; no longer J16.2 (+3V3), J17.3 (SPI_SCLK), J18.5 (+3V3), J20.2 (+3V3), J21.4 (GND), J23.2 (+3V3), R30.2 (+3V3), R31.2 (+3V3), R52.2 (+3V3), R53.1 (+3V3), TP_VIN.18 (SPI_MOSI), TP_VIN_PROT.3 (GND)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
- net +3V3_ANA: now also FB1.2 (+3V3_ANA), J16.4 (GND), J23.3 (ADS_AIN3), TP_3V3A.1 (+3V3_ANA), U5.1 (THERM_CH_4); no longer J15.4 (GND), J22.3 (ADS_AIN3), R54.1 (+3V3_ANA), U2.1 (THERM_CH_4)
- net +5V: now also J20.4 (GND), TP_5V.1 (+5V), U3.2 (+5V), U3.6 (3V3_BST); no longer J19.4 (GND), R55.1 (+5V), TP_VIN_PROT.2 (+5V), TP_VIN_PROT.6 (3V3_BST)
- net 3V3_BST: now also U3.4 (+5V); no longer TP_VIN_PROT.4 (+5V)
- net 3V3_SW: now also L1.1 (3V3_SW), U3.5 (3V3_SW); no longer J23.1 (3V3_SW), TP_VIN_PROT.5 (3V3_SW)
- net ADS_AIN0: now also TP_ADS_AIN0.1 (ADS_AIN0), U4.1 (GND); no longer TP_3V3.1 (ADS_AIN0), U1.1 (GND)
- net ADS_AIN1: now also TP_ADS_AIN1.1 (ADS_AIN1), U4.9 (I2C_SDA); no longer TP_3V3A.1 (ADS_AIN1), U1.9 (I2C_SDA)
- net ADS_AIN2: now also TP_ADS_AIN2.1 (ADS_AIN2), U4.8 (+3V3); no longer TP_5V.1 (ADS_AIN2), U1.8 (+3V3)
- net ADS_AIN3: now also J23.1 (+3V3_ANA), TP_ADS_AIN3.1 (ADS_AIN3), U4.7 (ADS_AIN3); no longer J22.1 (+3V3_ANA), TP_ADS_AIN0.1 (ADS_AIN3), U1.7 (ADS_AIN3)
- net AUX_ANALOG_IN: now also J16.1 (THERM_CH_5), J23.6 (I2C_SCL), TP_AUX_ANALOG.1 (AUX_ANALOG_IN); no longer J15.1 (THERM_CH_5), J22.6 (I2C_SCL), TP_ADS_AIN1.1 (AUX_ANALOG_IN)
- net AUX_IO0_THERMAL_CUTOFF_OK: now also J19.6 (GND), R47.1 (AUX_IO0_THERMAL_CUTOFF_OK), TP_CUTOFF.1 (AUX_IO0_THERMAL_CUTOFF_OK), U1.6 (THERM_MUX_S2); no longer J18.6 (GND), R45.1 (AUX_IO0_THERMAL_CUTOFF_OK), TP_CAM_PWDN.1 (AUX_IO0_THERMAL_CUTOFF_OK), TP_VIN.6 (THERM_MUX_S2)
- net CAM_CS_N: now also J18.7 (CAM_FRAME_INT), R42.1 (CAM_CS_N), TP_CAM_CS.1 (CAM_CS_N), U1.17 (SPI_SCLK); no longer J17.7 (CAM_FRAME_INT), R40.1 (CAM_CS_N), TP_ADS_AIN3.1 (CAM_CS_N), TP_VIN.17 (SPI_SCLK)
- net CAM_FRAME_INT: now also J18.6 (CAM_CS_N), TP_CAM_FRAME.1 (CAM_FRAME_INT), U1.16 (NC_16); no longer J17.6 (CAM_CS_N), TP_AUX_ANALOG.1 (CAM_FRAME_INT), TP_VIN.16 (NC_16)
- net CAM_PWDN_N: now also J18.4 (SPI_MOSI), TP_CAM_PWDN.1 (CAM_PWDN_N), U1.15 (NC_15); no longer J17.4 (SPI_MOSI), TP_BOOT.1 (CAM_PWDN_N), TP_VIN.15 (NC_15)
- net CAM_RESET_N: now also J18.5 (SPI_MISO), TP_CAM_RESET.1 (CAM_RESET_N), U1.30 (LID_CLOSED_N); no longer J17.5 (SPI_MISO), TP_CAM_CS.1 (CAM_RESET_N), TP_VIN.30 (LID_CLOSED_N)
- net CART_PRESENT_N: now also J19.2 (CART_PRESENT_N), R45.1 (CART_PRESENT_N), TP_CART.1 (CART_PRESENT_N), U1.7 (LED_EXC_PWM); no longer J18.2 (CART_PRESENT_N), R43.1 (CART_PRESENT_N), TP_CAM_FRAME.1 (CART_PRESENT_N), TP_VIN.7 (LED_EXC_PWM)
- net ESP_EN: now also J21.5 (ESP_EN), R48.1 (ESP_EN), TP_EN.1 (ESP_EN), U1.9 (HEATER_ARM); no longer J20.5 (ESP_EN), R46.1 (ESP_EN), TP_CAM_RESET.1 (ESP_EN), TP_VIN.9 (HEATER_ARM)
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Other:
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
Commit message: Reconcile Rev B ERC and fab release blockers
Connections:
- net +3V3: now also J18.1 (+3V3), J22.3 (+3V3), U1.2 (+3V3), U3.1 (+3V3), U4.8 (+3V3); no longer J18.3 (SPI_SCLK), J22.4 (GND), U1.18 (SPI_MOSI), U3.3 (GND), U4.6 (ADS_AIN2)
- net +3V3_ANA: now also J16.3 (+3V3_ANA), J23.1 (+3V3_ANA), U5.16 (+3V3_ANA); no longer J16.4 (GND), J23.3 (ADS_AIN3), U5.1 (THERM_CH_4)
- net +5V: now also J20.3 (+5V), U3.4 (+5V), U7.3 (+5V); no longer J20.4 (GND), U3.6 (3V3_BST)
- net 3V3_BST: now also U3.6 (3V3_BST); no longer U3.4 (+5V)
- net ADS_AIN0: now also U4.4 (ADS_AIN0); no longer U4.1 (GND)
- net ADS_AIN1: now also U4.5 (ADS_AIN1); no longer U4.9 (I2C_SDA)
- net ADS_AIN2: now also U4.6 (ADS_AIN2); no longer U4.8 (+3V3)
- net ADS_AIN3: now also J23.3 (ADS_AIN3); no longer J23.1 (+3V3_ANA)
- net AUX_ANALOG_IN: now also J16.2 (AUX_ANALOG_IN), J23.4 (AUX_ANALOG_IN); no longer J16.1 (THERM_CH_5), J23.6 (I2C_SCL)
- net AUX_IO0_THERMAL_CUTOFF_OK: now also J19.4 (AUX_IO0_THERMAL_CUTOFF_OK), U1.32 (AUX_IO0_THERMAL_CUTOFF_OK); no longer J19.6 (GND), U1.6 (THERM_MUX_S2)
- net CAM_CS_N: now also J18.6 (CAM_CS_N), U1.20 (CAM_CS_N); no longer J18.7 (CAM_FRAME_INT), U1.17 (SPI_SCLK)
- net CAM_FRAME_INT: now also J18.7 (CAM_FRAME_INT), U1.21 (CAM_FRAME_INT); no longer J18.6 (CAM_CS_N), U1.16 (NC_16)
- net CAM_PWDN_N: now also J18.9 (CAM_PWDN_N), U1.22 (CAM_PWDN_N); no longer J18.4 (SPI_MOSI), U1.15 (NC_15)
- net CAM_RESET_N: now also J18.8 (CAM_RESET_N), U1.8 (CAM_RESET_N); no longer J18.5 (SPI_MISO), U1.30 (LID_CLOSED_N)
- net CART_PRESENT_N: now also U1.31 (CART_PRESENT_N); no longer U1.7 (LED_EXC_PWM)
- net ESP_EN: now also U1.3 (ESP_EN); no longer U1.9 (HEATER_ARM)
- net ESP_GPIO0_BOOT: now also J21.6 (ESP_GPIO0_BOOT), U1.27 (ESP_GPIO0_BOOT); no longer J21.4 (UART0_RXD), U1.10 (HEATER0_PWM)
- net EXPOSURE_ACTIVE_IN: now also J17.4 (EXPOSURE_ACTIVE_IN), U1.29 (EXPOSURE_ACTIVE_IN); no longer J17.6 (SPARE_GPIO42)
- net FAN_PWM: now also J20.1 (FAN_PWM); no longer J20.2 (FAN_TACH)
- net FAN_TACH: now also J20.2 (FAN_TACH); no longer J20.1 (FAN_PWM)
- net FRAME_TRIG_OUT: now also J17.3 (FRAME_TRIG_OUT), U1.25 (FRAME_TRIG_OUT); no longer J17.1 (GND), U1.12 (THERM_MUX_EN_N)
- net GND: now also J1.13 (GND), J1.14 (GND), J1.15 (GND), J1.B12A1 (GND), J16.4 (GND), J17.1 (GND), J18.12 (GND), J18.2 (GND), J19.6 (GND), J20.4 (GND), J21.1 (GND), J22.4 (GND), Q1.3 (GND), Q2.3 (GND), U1.1 (GND), U1.40 (GND), U3.3 (GND), U4.1 (GND), U4.3 (GND), U5.7 (GND), U5.8 (GND), U6.3 (GND), U6.4 (GND), U7.2 (GND); no longer J1.A5 (USB_CC1), J1.A6 (USB_DP), J1.A7 (USB_DN), J1.B7 (USB_DN), J16.3 (+3V3_ANA), J17.3 (FRAME_TRIG_OUT), J18.10 (I2C_SDA), J18.11 (I2C_SCL), J19.4 (AUX_IO0_THERMAL_CUTOFF_OK), J20.3 (+5V), J21.3 (UART0_TXD), J22.3 (+3V3), U1.28 (LED_SYNC_OUT), U1.35 (SPARE_GPIO42), U3.1 (+3V3), U4.10 (I2C_SCL), U4.4 (ADS_AIN0), U5.3 (THERM_MUX_OUT), U5.4 (THERM_CH_7), U6.1 (HEATER_ARM), U6.2 (HEATER0_PWM), U7.1 (VIN_PROTECTED)
- net GND_EP: now also U1.41 (GND_EP); no longer U1.34 (STATUS_FAULT_LED)
- net HEATER0_GATE: now also Q1.1 (HEATER0_GATE), U6.7 (HEATER0_GATE); no longer Q1.2 (HEATER0_LOW), U6.6 (VDRV)
- net HEATER0_LOW: now also Q1.2 (HEATER0_LOW); no longer Q1.1 (HEATER0_GATE)
- net HEATER0_PWM: now also U1.10 (HEATER0_PWM), U6.2 (HEATER0_PWM); no longer U1.27 (ESP_GPIO0_BOOT), U6.3 (GND)
- net HEATER1_GATE: now also Q2.1 (HEATER1_GATE), U6.5 (HEATER1_GATE); no longer Q2.2 (HEATER1_LOW), U6.8 (HEATER1_PWM)
- net HEATER1_LOW: now also Q2.2 (HEATER1_LOW); no longer Q2.1 (HEATER1_GATE)
- net HEATER1_PWM: now also U1.11 (HEATER1_PWM), U6.8 (HEATER1_PWM); no longer U1.26 (NC_26), U6.5 (HEATER1_GATE)
- net HEATER_ARM: now also U1.9 (HEATER_ARM), U6.1 (HEATER_ARM); no longer U1.3 (ESP_EN), U6.4 (GND)
- net I2C_SCL: now also J18.11 (I2C_SCL), J22.2 (I2C_SCL), J23.6 (I2C_SCL), U4.10 (I2C_SCL); no longer J18.12 (GND), J22.1 (I2C_SDA), J23.4 (AUX_ANALOG_IN), U4.3 (GND)
- net I2C_SDA: now also J18.10 (I2C_SDA), J22.1 (I2C_SDA), U1.39 (I2C_SDA), U4.9 (I2C_SDA); no longer J18.2 (GND), J22.2 (I2C_SCL), U1.37 (UART0_TXD), U4.5 (ADS_AIN1)
- net LATCH_LOCKED_N: now also J19.3 (LATCH_LOCKED_N); no longer J19.1 (LID_CLOSED_N)
- net LED_CURRENT_SENSE: now also U10.4 (LED_CURRENT_SENSE)
- net LED_DIM_DRIVE: now also U8.22 (LED_DIM_DRIVE); no longer U8.7 (NC_7)
- net LED_DIM_GATE: now also U9.4 (LED_DIM_GATE)
- net LED_DRV_PLUS: now also U10.1 (LED_DRV_PLUS), U8.13 (LED_DRV_PLUS), U8.14 (LED_DRV_PLUS); no longer U10.3 (LED_PLUS), U8.15 (NC_15), U8.16 (NC_16)
- net LED_EXC_EN: now also U1.24 (LED_EXC_EN), U9.3 (LED_EXC_EN); no longer U1.13 (USB_DN), U9.1 (LED_EXC_PWM)
- net LED_EXC_PWM: now also U1.7 (LED_EXC_PWM), U9.1 (LED_EXC_PWM); no longer U1.31 (CART_PRESENT_N), U9.3 (LED_EXC_EN)
- net LED_MINUS: now also U8.11 (LED_MINUS), U8.12 (LED_MINUS); no longer U8.17 (NC_17), U8.18 (NC_18)
- net LED_PLUS: now also U10.3 (LED_PLUS); no longer U10.1 (LED_DRV_PLUS)
- net LED_SUPPLY: now also U8.23 (LED_SUPPLY), U8.24 (LED_SUPPLY); no longer U8.5 (NC_5), U8.6 (NC_6)
- net LED_SYNC_OUT: now also U1.28 (LED_SYNC_OUT); no longer U1.1 (GND)
- net LID_CLOSED_N: now also J19.1 (LID_CLOSED_N), U1.30 (LID_CLOSED_N); no longer J19.3 (LATCH_LOCKED_N), U1.8 (CAM_RESET_N)
- net SD_CS_N: now also U1.23 (SD_CS_N); no longer U1.14 (USB_DP)
- net SPARE_GPIO42: now also J17.6 (SPARE_GPIO42), U1.35 (SPARE_GPIO42); no longer J17.4 (EXPOSURE_ACTIVE_IN), U1.40 (GND)
- net SPI_MISO: now also J18.5 (SPI_MISO); no longer J18.8 (CAM_RESET_N)
- net SPI_MOSI: now also J18.4 (SPI_MOSI), U1.18 (SPI_MOSI); no longer J18.9 (CAM_PWDN_N), U1.2 (+3V3)
- net SPI_SCLK: now also J18.3 (SPI_SCLK), U1.17 (SPI_SCLK); no longer J18.1 (+3V3), U1.20 (CAM_CS_N)
- net STATUS_FAULT_LED: now also U1.34 (STATUS_FAULT_LED); no longer U1.41 (GND_EP)
- net STATUS_RUN_LED: now also U1.33 (STATUS_RUN_LED); no longer U1.5 (THERM_MUX_S1)
- net THERM_CH_0: now also U5.13 (THERM_CH_0); no longer U5.12 (THERM_CH_3)
- net THERM_CH_1: now also U5.14 (THERM_CH_1); no longer U5.11 (THERM_MUX_S0)
- net THERM_CH_2: now also U5.15 (THERM_CH_2); no longer U5.10 (THERM_MUX_S1)
- net THERM_CH_3: now also U5.12 (THERM_CH_3); no longer U5.13 (THERM_CH_0)
- net THERM_CH_4: now also U5.1 (THERM_CH_4); no longer U5.16 (+3V3_ANA)
- net THERM_CH_5: now also J16.1 (THERM_CH_5), U5.5 (THERM_CH_5); no longer J16.2 (AUX_ANALOG_IN), U5.6 (THERM_MUX_EN_N)
- net THERM_CH_6: now also U5.2 (THERM_CH_6); no longer U5.9 (THERM_MUX_S2)
- net THERM_CH_7: now also U5.4 (THERM_CH_7); no longer U5.7 (GND)
- net THERM_MUX_EN_N: now also U1.12 (THERM_MUX_EN_N), U5.6 (THERM_MUX_EN_N); no longer U1.25 (FRAME_TRIG_OUT), U5.5 (THERM_CH_5)
- net THERM_MUX_OUT: now also U5.3 (THERM_MUX_OUT); no longer U5.8 (GND)
- net THERM_MUX_S0: now also U1.4 (THERM_MUX_S0), U5.11 (THERM_MUX_S0); no longer U1.36 (UART0_RXD), U5.14 (THERM_CH_1)
- net THERM_MUX_S1: now also U1.5 (THERM_MUX_S1), U5.10 (THERM_MUX_S1); no longer U1.33 (STATUS_RUN_LED), U5.15 (THERM_CH_2)
- net THERM_MUX_S2: now also U1.6 (THERM_MUX_S2), U5.9 (THERM_MUX_S2); no longer U1.32 (AUX_IO0_THERMAL_CUTOFF_OK), U5.2 (THERM_CH_6)
- net UART0_RXD: now also J21.4 (UART0_RXD), U1.36 (UART0_RXD); no longer J21.6 (ESP_GPIO0_BOOT), U1.4 (THERM_MUX_S0)
- net UART0_TXD: now also J21.3 (UART0_TXD), U1.37 (UART0_TXD); no longer J21.1 (GND), U1.39 (I2C_SDA)
- net USB_CC1: now also J1.A5 (USB_CC1); no longer J1.15 (GND)
- net USB_CC2: now also J1.B5 (USB_CC2); no longer J1.B6 (USB_DP)
- net USB_DN: now also J1.A7 (USB_DN), J1.B7 (USB_DN), U1.13 (USB_DN), U2.3 (USB_DN), U2.4 (USB_DN); no longer J1.13 (GND), J1.B12A1 (GND), U1.24 (LED_EXC_EN), U2.1 (USB_DP), U2.6 (USB_DP)
- net USB_DP: now also J1.A6 (USB_DP), J1.B6 (USB_DP), U1.14 (USB_DP), U2.1 (USB_DP), U2.6 (USB_DP); no longer J1.14 (GND), J1.B5 (USB_CC2), U1.23 (SD_CS_N), U2.3 (USB_DN), U2.4 (USB_DN)
- net VBUS: now also J1.A9B4 (VBUS), J1.B9A4 (VBUS); no longer J1.A8 (NC_A8), J1.B8 (NC_B8)
- net VDRV: now also U6.6 (VDRV); no longer U6.7 (HEATER0_GATE)
- net VIN_PROTECTED: now also U7.1 (VIN_PROTECTED); no longer U7.2 (GND)
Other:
- moved on the sheet: C1, C10, C11, C12, C13, C14, C15, C16, C17, C2, C3, C4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
